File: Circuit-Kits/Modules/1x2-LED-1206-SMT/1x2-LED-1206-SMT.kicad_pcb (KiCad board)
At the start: 2 copper layers, 15.7 x 7.8 mm, 1 part

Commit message: Add Dwgs.User layer to all KiCad files.
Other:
- board text added: "FABRICATION NOTES 1. MATERIAL .062 INCH +/- 10% THICK FR4. 1 OZ COPPER. 2. BOARDS SHALL BE ROHS COMPLIANT. 3. MANUFACTURE IN ACCORDANCE WITH IPC-6012 CLASS 2 4. MAXIMUM HOLE PLACEMENT TOLERANCE OF +/- 0.003 INCH 5. MAXIMUM HOLE DIAMETER TOLERNACE OF +/- 0.003 INCH AFTER PLATING 6. BOTH SIDES OF THE BOARD SHALL HAVE SOLDER MASK (ANY COLOR) OVER BARE COPPER. 7. BOTH SIDES OF THE BOARD SHALL HAVE WH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"
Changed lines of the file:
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@@
     (area 104.572999 74.854999 178.510001 123.265001)
     (thickness 1.6)
-    (drawings 17)
+    (drawings 1)
     (tracks 0)
     (zones 0)
@@
     (title "1x2 LED 1206 SMT Module")
     (date "31 Jan 2017")
-    (rev "v1.1")
+    (rev 1.0)
     (company "All rights reserved.")
-    (comment 1 "help@browndoggadgets.com")
-    (comment 2 "http://browndoggadgets.com/")
+    (comment 1 help@browndoggadgets.com)
+    (comment 2 http://browndoggadgets.com/)
     (comment 3 "Brown Dog Gadgets")
   )
@@
     (38 B.Mask user)
     (39 F.Mask user)
+    (40 Dwgs.User user)
+    (40 Dwgs.User user)
     (44 Edge.Cuts user)
     (46 B.CrtYd user)
@@
       (net 2 VCC))
   )
-  (gr_circle (center 117.348 76.962) (end 118.618 76.962) (layer Dwgs.User) (width 0.15))
-  (gr_line (start 114.427 78.994) (end 114.427 74.93) (angle 90) (layer Dwgs.User) (width 0.15))
-  (gr_line (start 120.269 78.994) (end 114.427 78.994) (angle 90) (layer Dwgs.User) (width 0.15))
-  (gr_line (start 120.269 74.93) (end 120.269 78.994) (angle 90) (layer Dwgs.User) (width 0.15))
-  (gr_line (start 114.427 74.93) (end 120.269 74.93) (angle 90) (layer Dwgs.User) (width 0.15))
-  (gr_line (start 120.523 93.98) (end 104.648 93.98) (angle 90) (layer Dwgs.User) (width 0.15))
-  (gr_line (start 173.355 102.235) (end 173.355 94.615) (angle 90) (layer Dwgs.User) (width 0.15))
-  (gr_line (start 178.435 102.235) (end 173.355 102.235) (angle 90) (layer Dwgs.User) (width 0.15))
-  (gr_line (start 178.435 94.615) (end 178.435 102.235) (angle 90) (layer Dwgs.User) (width 0.15))
-  (gr_line (start 173.355 94.615) (end 178.435 94.615) (angle 90) (layer Dwgs.User) (width 0.15))
-  (gr_line (start 109.093 123.19) (end 109.093 114.3) (angle 90) (layer Dwgs.User) (width 0.15))
-  (gr_line (start 122.428 123.19) (end 109.093 123.19) (angle 90) (layer Dwgs.User) (width 0.15))
-  (gr_line (start 122.428 114.3) (end 122.428 123.19) (angle 90) (layer Dwgs.User) (width 0.15))
-  (gr_line (start 109.093 114.3) (end 122.428 114.3) (angle 90) (layer Dwgs.User) (width 0.15))
-  (gr_line (start 104.648 93.98) (end 104.648 82.55) (angle 90) (layer Dwgs.User) (width 0.15))
-  (gr_line (start 120.523 82.55) (end 120.523 93.98) (angle 90) (layer Dwgs.User) (width 0.15))
-  (gr_line (start 104.648 82.55) (end 120.523 82.55) (angle 90) (layer Dwgs.User) (width 0.15))
+  (gr_text "FABRICATION NOTES\n\n1. MATERIAL .062 INCH +/- 10% THICK FR4. 1 OZ COPPER. \n2. BOARDS SHALL BE ROHS COMPLIANT. \n3. MANUFACTURE IN ACCORDANCE WITH IPC-6012 CLASS 2\n4. MAXIMUM HOLE PLACEMENT TOLERANCE OF +/- 0.003 INCH\n5. MAXIMUM HOLE DIAMETER TOLERNACE OF +/- 0.003 INCH AFTER PLATING\n6. BOTH SIDES OF THE BOARD SHALL HAVE SOLDER MASK (ANY COLOR) OVER BARE COPPER. \n7. BOTH SIDES OF THE BOARD SHALL HAVE WHITE SILKSCREEN. DO NOT PLACE SILK OVER BARE COPPER.\n8. BOARDS SHALL HAVE ENIG FINISH.\n9. MINIMUM TRACE WIDTH - 0.006 INCH\n   MINIMUM SPACE - 0.006 INCH\n   MINIMUM HOLE DIA - 0.013 INCH " (at 155.194 101.346) (layer Dwgs.User)
+    (effects (font (size 1.016 1.016) (thickness 0.1524)) (justify left))
+  )
 )

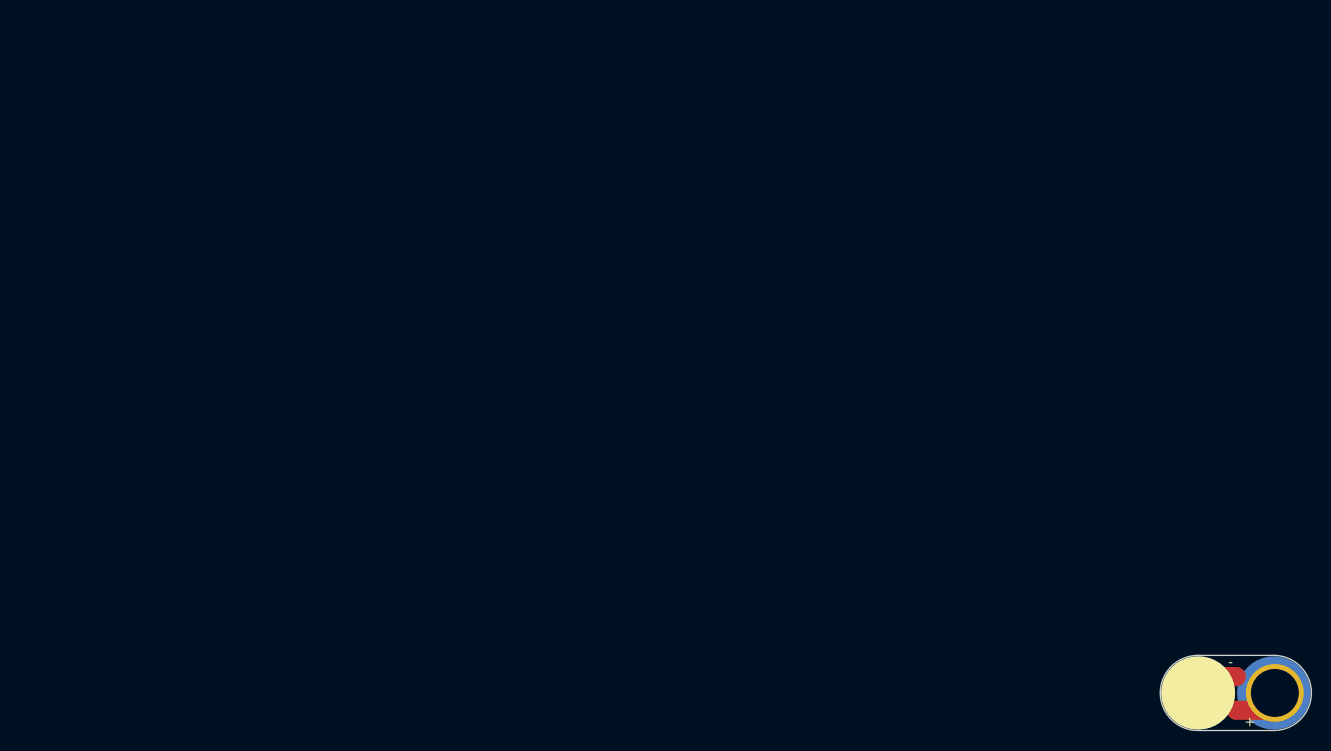
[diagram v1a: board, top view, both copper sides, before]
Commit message: Public release of 1x2-LED-1206-SMT
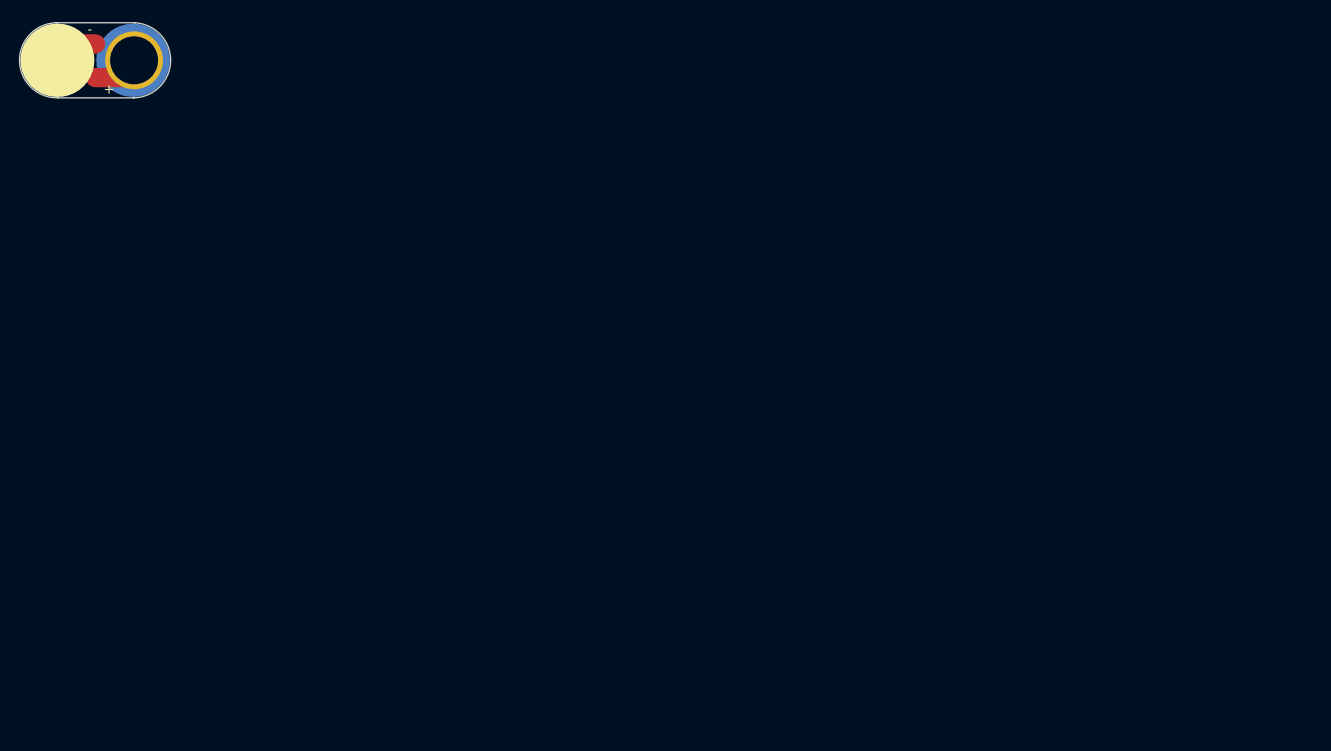
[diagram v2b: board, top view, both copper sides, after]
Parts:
- moved LED1 135.4 mm to (18.6, 32.3)
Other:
- board text added: "FABRICATION NOTES 1. MATERIAL .062 INCH +/- 10% THICK FR4. 1 OZ COPPER. 2. BOARDS SHALL BE ROHS COMPLIANT. 3. MANUFACTURE IN ACCORDANCE WITH IPC-6012 CLASS 2 4. MAXIMUM HOLE PLACEMENT TOLERANCE OF +/- 0.003 INCH 5. MAXIMUM HOLE DIAMETER TOLERNACE OF +/- 0.003 INCH AFTER PLATING 6. BOTH SIDES OF THE BOARD SHALL HAVE SOLDER MASK (BLACK) OVER BARE COPPER. 7. BOTH SIDES OF THE BOARD SHALL HAVE WHITE 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"
- board text removed: "FABRICATION NOTES 1. MATERIAL .062 INCH +/- 10% THICK FR4. 1 OZ COPPER. 2. BOARDS SHALL BE ROHS COMPLIANT. 3. MANUFACTURE IN ACCORDANCE WITH IPC-6012 CLASS 2 4. MAXIMUM HOLE PLACEMENT TOLERANCE OF +/- 0.003 INCH 5. MAXIMUM HOLE DIAMETER TOLERNACE OF +/- 0.003 INCH AFTER PLATING 6. BOTH SIDES OF THE BOARD SHALL HAVE SOLDER MASK (ANY COLOR) OVER BARE COPPER. 7. BOTH SIDES OF THE BOARD SHALL HAVE WH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"
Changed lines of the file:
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@@
     (links 2)
     (no_connects 2)
-    (area 104.572999 74.854999 178.510001 123.265001)
+    (area 132.864397 90.5002 236.473996 112.2934)
     (thickness 1.6)
     (drawings 1)
@@
     (38 B.Mask user)
     (39 F.Mask user)
-    (40 Dwgs.User user)
     (40 Dwgs.User user)
     (44 Edge.Cuts user)
@@
   )
   (module Crazy_Circuits:LED-SMT-1206-1x2-UNLIMITED (layer F.Cu)
-    (at 137.04 98.03)
+    (at 18.5998 32.3456)
     (descr "1206 surface mount centered 1x2")
     (fp_text reference LED1 (at 4.6 -3) (layer B.SilkS) hide
@@
       (net 2 VCC))
   )
-  (gr_text "FABRICATION NOTES\n\n1. MATERIAL .062 INCH +/- 10% THICK FR4. 1 OZ COPPER. \n2. BOARDS SHALL BE ROHS COMPLIANT. \n3. MANUFACTURE IN ACCORDANCE WITH IPC-6012 CLASS 2\n4. MAXIMUM HOLE PLACEMENT TOLERANCE OF +/- 0.003 INCH\n5. MAXIMUM HOLE DIAMETER TOLERNACE OF +/- 0.003 INCH AFTER PLATING\n6. BOTH SIDES OF THE BOARD SHALL HAVE SOLDER MASK (ANY COLOR) OVER BARE COPPER. \n7. BOTH SIDES OF THE BOARD SHALL HAVE WHITE SILKSCREEN. DO NOT PLACE SILK OVER BARE COPPER.\n8. BOARDS SHALL HAVE ENIG FINISH.\n9. MINIMUM TRACE WIDTH - 0.006 INCH\n   MINIMUM SPACE - 0.006 INCH\n   MINIMUM HOLE DIA - 0.013 INCH " (at 155.194 101.346) (layer Dwgs.User)
-    (effects (font (size 1.016 1.016) (thickness 0.1524)) (justify left))
+  (gr_text "FABRICATION NOTES\n\n1. MATERIAL .062 INCH +/- 10% THICK FR4. 1 OZ COPPER. \n2. BOARDS SHALL BE ROHS COMPLIANT. \n3. MANUFACTURE IN ACCORDANCE WITH IPC-6012 CLASS 2\n4. MAXIMUM HOLE PLACEMENT TOLERANCE OF +/- 0.003 INCH\n5. MAXIMUM HOLE DIAMETER TOLERNACE OF +/- 0.003 INCH AFTER PLATING\n6. BOTH SIDES OF THE BOARD SHALL HAVE SOLDER MASK (BLACK) OVER BARE COPPER. \n7. BOTH SIDES OF THE BOARD SHALL HAVE WHITE SILKSCREEN. DO NOT PLACE SILK OVER BARE COPPER.\n8. BOARDS SHALL HAVE ENIG FINISH.\n9. MINIMUM TRACE WIDTH - 0.006 INCH\n   MINIMUM SPACE - 0.006 INCH\n   MINIMUM HOLE DIA - 0.013 INCH " (at 0.8636 86.4616) (layer Dwgs.User)
+    (effects (font (size 2.54 2.54) (thickness 0.254)) (justify left))
   )
 )
